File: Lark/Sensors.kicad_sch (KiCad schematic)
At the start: 36 parts, among them U1 MIC7211YM5-TR, U2 MIC7211YM5-TR, U3 MIC7211YM5-TR, U4 MIC7211YM5-TR

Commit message: still porting design over from 'other' cad software.
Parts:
- TP1, TP2, TP3, TP4, TP5, TP6: footprint (none) -> TestPoint:TestPoint_Pad_D1.0mm
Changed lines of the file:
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@@
 			)
 		)
-		(property "Footprint" ""
+		(property "Footprint" "TestPoint:TestPoint_Pad_D1.0mm"
 			(at 181.61 45.72 0)
 			(effects
@@
 			)
 		)
-		(property "Footprint" ""
+		(property "Footprint" "TestPoint:TestPoint_Pad_D1.0mm"
 			(at 161.29 53.34 0)
 			(effects
@@
 			)
 		)
-		(property "Footprint" ""
+		(property "Footprint" "TestPoint:TestPoint_Pad_D1.0mm"
 			(at 161.29 123.19 0)
 			(effects
@@
 			)
 		)
-		(property "Footprint" ""
+		(property "Footprint" "TestPoint:TestPoint_Pad_D1.0mm"
 			(at 181.61 115.57 0)
 			(effects
@@
 			)
 		)
-		(property "Footprint" ""
+		(property "Footprint" "TestPoint:TestPoint_Pad_D1.0mm"
 			(at 54.61 43.18 0)
 			(effects
@@
 			)
 		)
-		(property "Footprint" ""
+		(property "Footprint" "TestPoint:TestPoint_Pad_D1.0mm"
 			(at 54.61 113.03 0)
 			(effects

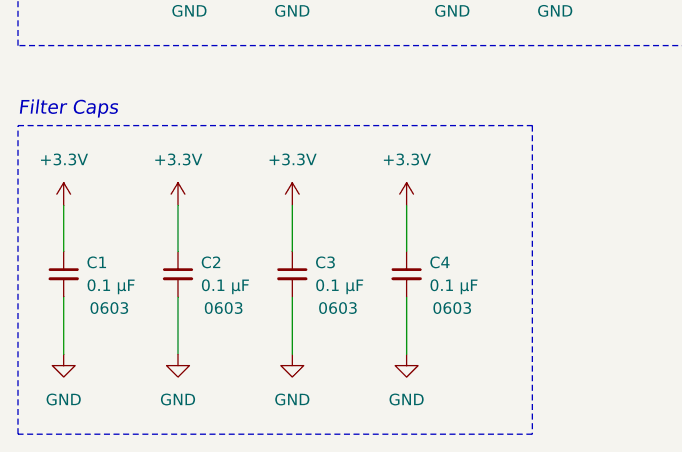
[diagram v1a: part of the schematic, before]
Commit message: added power section to schematic
It needs revised, due to thermal issue. Specifically in regards to my soft start circuit, the mosfet wont be able to handle the power dissipated during a slow turn on.
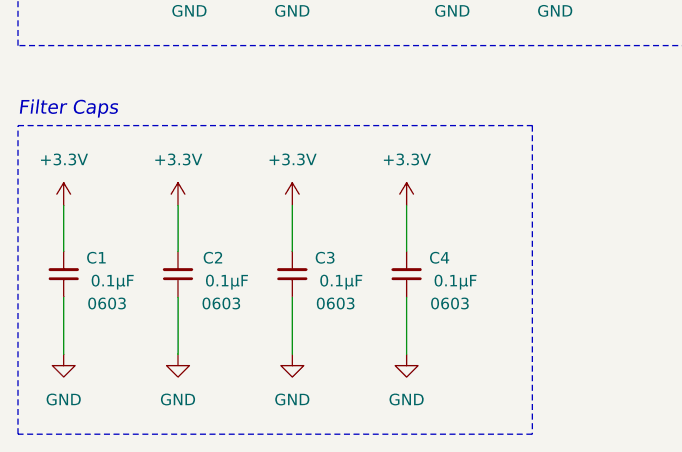
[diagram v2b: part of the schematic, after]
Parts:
- C1, C2, C3, C4: value 0.1 µF -> 0.1µF
- D1, D2, D3, D4: footprint onsemi:D_SOD-523 -> onsemi:ESD5Z3.3T1G
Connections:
- net +3.3V: now also C1.2, C2.2, C3.2, C4.2; no longer C1.1, C2.1, C3.1, C4.1
- net GND: now also C1.1, C2.1, C3.1, C4.1; no longer C1.2, C2.2, C3.2, C4.2

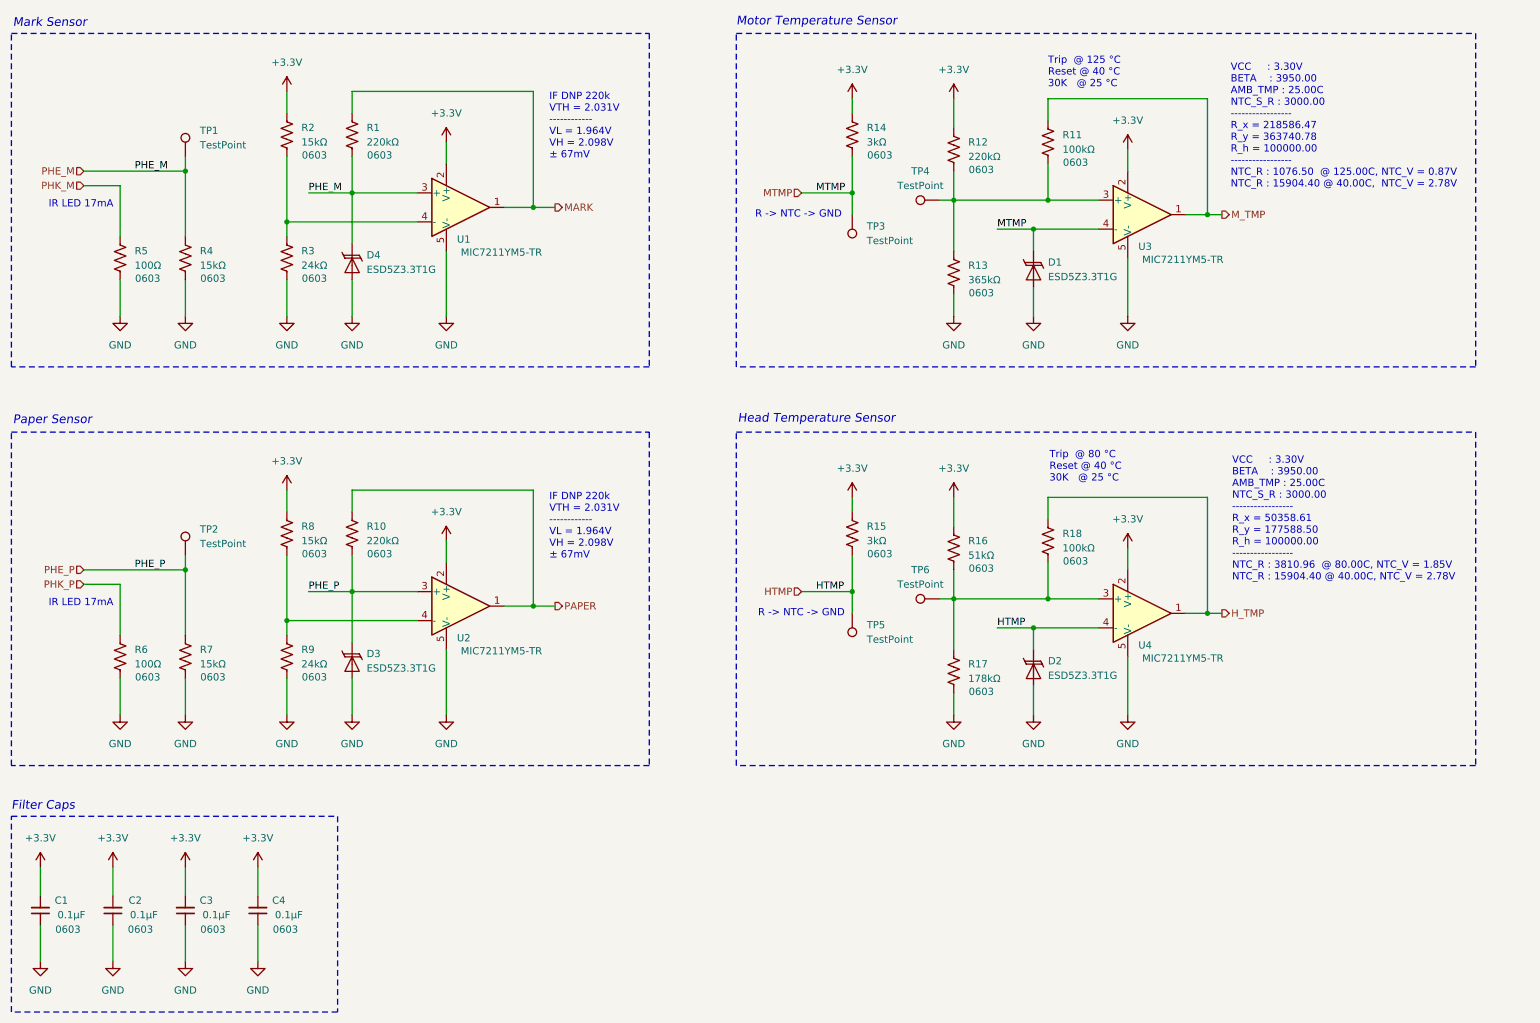
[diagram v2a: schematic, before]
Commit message: update, WIP
- Reannotated schematic.
- Added STM32 device.
- Fixed High-side switch (removed soft-start cap for device safety).
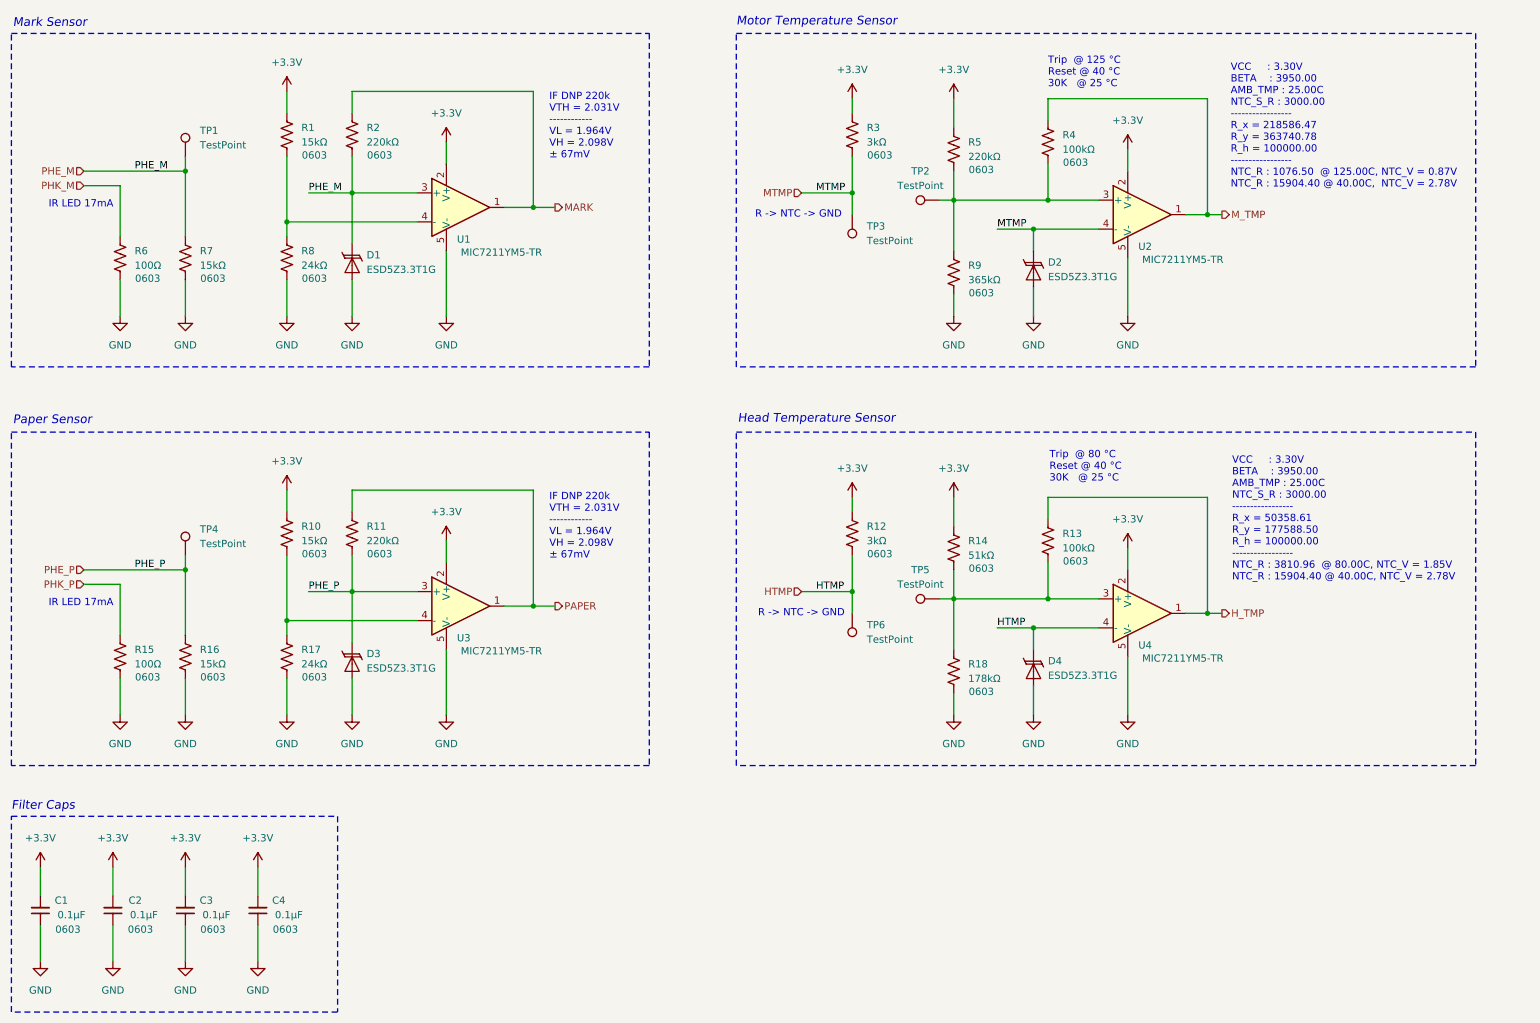
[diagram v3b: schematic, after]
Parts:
- renumbered D4 to D1, D1 to D2, D2 to D4, R2 to R1, R8 to R10, R10 to R11, R15 to R12, R18 to R13, R16 to R14, R6 to R15, R7 to R16, R9 to R17, R17 to R18, R1 to R2, R14 to R3, R11 to R4, R12 to R5, R5 to R6, R4 to R7, R3 to R8, R13 to R9, TP4 to TP2, TP2 to TP4, TP6 to TP5, TP5 to TP6, U3 to U2, U2 to U3

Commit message: Updated schematic, WIP
- Added NOR flash part.
- Added new CubeMX config file.
- Reannotated the schematic.
- Made some more connections to the MCU.
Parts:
- added R19: 0R, Stackpole:R_0603, symbol Stackpole:Resistor
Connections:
- net HTMP: now also R19.2
- new net HTMP_RAW: R19.1
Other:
- note added: "ADC Jumper"
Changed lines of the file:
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@@
 	)
 	(rectangle
+		(start 80.01 180.34)
+		(end 120.65 193.04)
+		(stroke
+			(width 0)
+			(type dash)
+		)
+		(fill
+			(type none)
+		)
+	)
+	(rectangle
 		(start 19.05 91.44)
 		(end 130.81 149.86)
@@
 		)
 	)
+	(text "ADC Jumper"
+		(exclude_from_sim no)
+		(at 80.01 178.816 0)
+		(effects
+			(font
+				(size 1.524 1.524)
+				(italic yes)
+			)
+			(justify left)
+		)
+	)
 	(text "Mark Sensor"
 		(exclude_from_sim no)
@@
 	(wire
 		(pts
+			(xy 105.41 185.42) (xy 114.3 185.42)
+		)
+		(stroke
+			(width 0)
+			(type default)
+		)
+	)
+	(wire
+		(pts
 			(xy 166.37 33.02) (xy 166.37 35.56)
 		)
@@
 	(wire
 		(pts
+			(xy 93.98 185.42) (xy 97.79 185.42)
+		)
+		(stroke
+			(width 0)
+			(type default)
+		)
+	)
+	(wire
+		(pts
 			(xy 184.15 50.8) (xy 184.15 59.69)
 		)
@@
 		)
 	)
+	(label "HTMP"
+		(at 114.3 185.42 180)
+		(effects
+			(font
+				(size 1.27 1.27)
+			)
+			(justify right bottom)
+		)
+	)
 	(label "PHE_M"
 		(at 71.12 49.53 0)
@@
 		)
 	)
+	(hierarchical_label "HTMP_RAW"
+		(shape output)
+		(at 93.98 185.42 180)
+		(effects
+			(font
+				(size 1.27 1.27)
+			)
+			(justify right)
+		)
+	)
 	(hierarchical_label "MTMP"
 		(shape input)
@@
 					(unit 1)
 				)
+			)
+		)
+	)
+	(symbol
+		(lib_id "Stackpole:Resistor")
+		(at 101.6 185.42 90)
+		(unit 1)
+		(exclude_from_sim no)
+		(in_bom yes)
+		(on_board yes)
+		(dnp yes)
+		(property "Reference" "R19"
+			(at 102.616 182.88 90)
+			(effects
+				(font
+					(size 1.27 1.27)
+				)
+				(justify left)
+			)
+		)
+		(property "Value" "0R"
+			(at 101.346 188.214 90)
+			(effects
+				(font
+					(size 1.27 1.27)
+				)
+				(justify left)
+			)
+		)
+		(property "Footprint" "Stackpole:R_0603"
+			(at 101.854 184.404 90)
+			(effects
+				(font
+					(size 1.27 1.27)
+				)
+				(hide yes)
+			)
+		)
+		(property "Datasheet" "~"
+			(at 101.6 185.42 0)
+			(effects
+				(font
+					(size 1.27 1.27)
+				)
+				(hide yes)
+			)
+		)
+		(property "Description" "Resistor, US symbol"
+			(at 101.6 185.42 0)
+			(effects
+				(font
+					(size 1.27 1.27)
+				)
+				(hide yes)
+			)
+		)
+		(property "Power" "1/10W"
+			(at 105.156 179.832 0)
+			(effects
+				(font
+					(size 1.27 1.27)
+				)
+				(hide yes)
+			)
+		)
+		(property "Case" "0603"
+			(at 101.092 190.246 90)
+			(effects
+				(font
+					(size 1.27 1.27)
+				)
+			)
+		)
+		(property "MPN" "RMCF0603ZT0R00"
+			(at 101.6 185.42 0)
+			(effects
+				(font
+					(size 1.27 1.27)
+				)
+				(hide yes)
+			)
+		)
+		(pin "1"
+		)
+		(pin "2"
+		)
+		(instances
+			(project "Lark"
+				(path "/a351af57-4353-47da-9f45-7393de572768/e3e99bd1-20bf-4506-a33a-c7e187c8429b"
+					(reference "R19")
+					(unit 1)
+				)

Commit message: Changed revision again...
- It dawned on me that this is rev 2, so the rev is now 01.00.1.
- Added thermal relief to the TH pads so I can actually solder the parts.
- Added more silkscreen to denote the rev, the github link, and ESD sensitivity of the device.
- Made minor pcb changes, I moved a test point, and cleaned up some traces.
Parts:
- R19, TP1, TP2, TP3, TP4, TP5, TP6: now left out of the parts list
